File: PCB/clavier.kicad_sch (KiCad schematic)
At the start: 0 parts

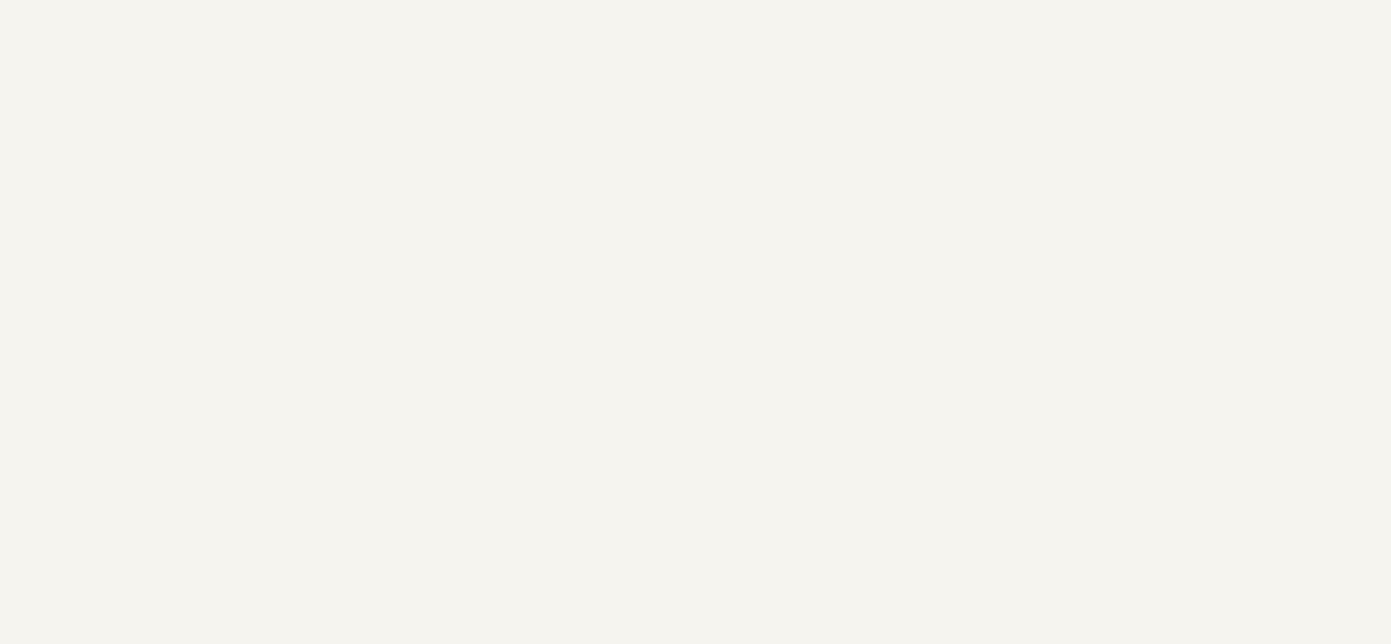
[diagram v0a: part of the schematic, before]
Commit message: Move the PCB files to a subfolder
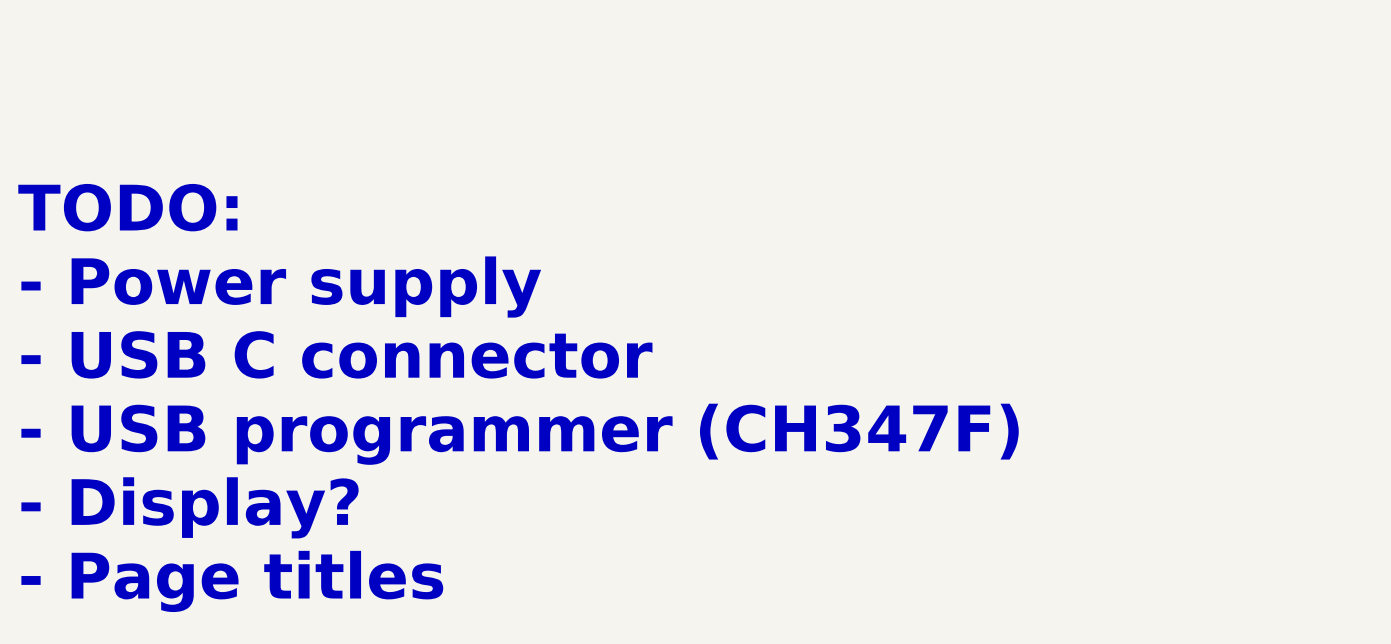
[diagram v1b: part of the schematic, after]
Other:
- note added: "TODO: - Power supply - USB C connector - USB programmer (CH347F) - Display? - Page titles"
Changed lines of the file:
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@@
 	(generator_version "9.0")
 	(paper "A4")
+	(text "TODO:\n- Power supply\n- USB C connector\n- USB programmer (CH347F)\n- Display?\n- Page titles"
+		(exclude_from_sim no)
+		(at 40.0 150.0 0)
+		(effects
+			(font
+				(size 5.08 5.08)
+				(thickness 1.016)
+				(bold yes)
+				(color 194 0 0 1)
+			)
+			(justify left)
+		)
+	)
 	(bus
 		(pts

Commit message: Add more TODOs
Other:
- added sheet Display (display.kicad_sch)
- added sheet Power (power.kicad_sch)
- added sheet USB (usb.kicad_sch)
- note added: "TODO schematics: - Power supply - LEDs - Test points - USB C connector - USB hub (GL852G-OHY60) - USB programmer (CH347F) - Display? - Page titles - Check licenses TODO layout: - Mounting holes - 3D models (all, including keycaps) - Alternate ctrl + odd/even number keys - Cat logo - Title block TODO release: - Export production files - Export PDF"
- note removed: "TODO: - Power supply - USB C connector - USB programmer (CH347F) - Display? - Page titles"
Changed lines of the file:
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@@
 	(generator_version "9.0")
 	(paper "A4")
-	(text "TODO:\n- Power supply\n- USB C connector\n- USB programmer (CH347F)\n- Display?\n- Page titles"
-		(exclude_from_sim no)
-		(at 40.0 150.0 0)
+	(text "TODO schematics:\n- Power supply\n- LEDs\n- Test points\n- USB C connector\n- USB hub (GL852G-OHY60)\n- USB programmer (CH347F)\n- Display?\n- Page titles\n- Check licenses\n\nTODO layout:\n- Mounting holes\n- 3D models (all, including keycaps)\n- Alternate ctrl + odd/even number keys\n- Cat logo\n- Title block\n\nTODO release:\n- Export production files\n- Export PDF"
+		(exclude_from_sim no)
+		(at 19.304 99.568 0)
 		(effects
 			(font
@@
 	(bus
 		(pts
-			(xy 127 80.01) (xy 165.1 80.01)
+			(xy 177.8 92.71) (xy 215.9 92.71)
 		)
 		(stroke
@@
 	(bus
 		(pts
-			(xy 127 85.09) (xy 165.1 85.09)
+			(xy 177.8 97.79) (xy 215.9 97.79)
 		)
 		(stroke
@@
 	)
 	(sheet
-		(at 165.1 76.2)
+		(at 190.5 38.1)
+		(size 12.7 12.7)
+		(exclude_from_sim no)
+		(in_bom yes)
+		(on_board yes)
+		(dnp no)
+		(fields_autoplaced yes)
+		(stroke
+			(width 0.1524)
+			(type solid)
+		)
+		(fill
+			(color 0 0 0 0.0000)
+		)
+		(property "Sheetname" "Power"
+			(at 190.5 37.3884 0)
+			(effects
+				(font
+					(size 1.27 1.27)
+				)
+				(justify left bottom)
+			)
+		)
+		(property "Sheetfile" "power.kicad_sch"
+			(at 190.5 51.3846 0)
+			(effects
+				(font
+					(size 1.27 1.27)
+				)
+				(justify left top)
+			)
+		)
+		(instances
+			(project "clavier"
+				(path "/6362c6e0-59ef-40d3-b6e0-7e9dfe7b9b20"
+					(page "8")
+				)
+			)
+		)
+	)
+	(sheet
+		(at 215.9 38.1)
+		(size 12.7 12.7)
+		(exclude_from_sim no)
+		(in_bom yes)
+		(on_board yes)
+		(dnp no)
+		(fields_autoplaced yes)
+		(stroke
+			(width 0.1524)
+			(type solid)
+		)
+		(fill
+			(color 0 0 0 0.0000)
+		)
+		(property "Sheetname" "Display"
+			(at 215.9 37.3884 0)
+			(effects
+				(font
+					(size 1.27 1.27)
+				)
+				(justify left bottom)
+			)
+		)
+		(property "Sheetfile" "display.kicad_sch"
+			(at 215.9 51.3846 0)
+			(effects
+				(font
+					(size 1.27 1.27)
+				)
+				(justify left top)
+			)
+		)
+		(instances
+			(project "clavier"
+				(path "/6362c6e0-59ef-40d3-b6e0-7e9dfe7b9b20"
+					(page "7")
+				)
+			)
+		)
+	)
+	(sheet
+		(at 215.9 88.9)
 		(size 25.4 12.7)
 		(exclude_from_sim no)
@@
 		)
 		(property "Sheetname" "FPGA"
-			(at 165.1 75.4884 0)
+			(at 215.9 88.1884 0)
 			(effects
 				(font
@@
 		)
 		(property "Sheetfile" "fpga.kicad_sch"
-			(at 165.1 89.4846 0)
+			(at 215.9 102.1846 0)
 			(effects
 				(font
@@
 		)
 		(pin "K{Keys}" input
-			(at 165.1 80.01 180)
+			(at 215.9 92.71 180)
 			(effects
 				(font
@@
 		)
 		(pin "Kp{KpKeys}" input
-			(at 165.1 85.09 180)
+			(at 215.9 97.79 180)
 			(effects
 				(font
@@
 			(project "clavier"
 				(path "/6362c6e0-59ef-40d3-b6e0-7e9dfe7b9b20"
+					(page "3")
+				)
+			)
+		)
+	)
+	(sheet
+		(at 165.1 38.1)
+		(size 12.7 12.7)
+		(exclude_from_sim no)
+		(in_bom yes)
+		(on_board yes)
+		(dnp no)
+		(fields_autoplaced yes)
+		(stroke
+			(width 0.1524)
+			(type solid)
+		)
+		(fill
+			(color 0 0 0 0.0000)
+		)
+		(property "Sheetname" "USB"
+			(at 165.1 37.3884 0)
+			(effects
+				(font
+					(size 1.27 1.27)
+				)
+				(justify left bottom)
+			)
+		)
+		(property "Sheetfile" "usb.kicad_sch"
+			(at 165.1 51.3846 0)
+			(effects
+				(font
+					(size 1.27 1.27)
+				)
+				(justify left top)
+			)
+		)
+		(instances
+			(project "clavier"
+				(path "/6362c6e0-59ef-40d3-b6e0-7e9dfe7b9b20"
 					(page "2")
 				)
@@
 	)
 	(sheet
-		(at 101.6 76.2)
+		(at 152.4 88.9)
 		(size 25.4 12.7)
 		(exclude_from_sim no)
@@
 		)
 		(property "Sheetname" "Keys"
-			(at 101.6 75.4884 0)
+			(at 152.4 88.1884 0)
 			(effects
 				(font
@@
 		)
 		(property "Sheetfile" "keys.kicad_sch"
-			(at 101.6 89.4846 0)
+			(at 152.4 102.1846 0)
 			(effects
 				(font
@@
 		)
 		(pin "Kp{KpKeys}" output
-			(at 127 85.09 0)
+			(at 177.8 97.79 0)
 			(effects
 				(font
@@
 		)
 		(pin "K{Keys}" output
-			(at 127 80.01 0)
+			(at 177.8 92.71 0)
 			(effects
 				(font
@@
 			(project "clavier"
 				(path "/6362c6e0-59ef-40d3-b6e0-7e9dfe7b9b20"
-					(page "5")
-				)
-			)
+					(page "6")
+				)
+			)

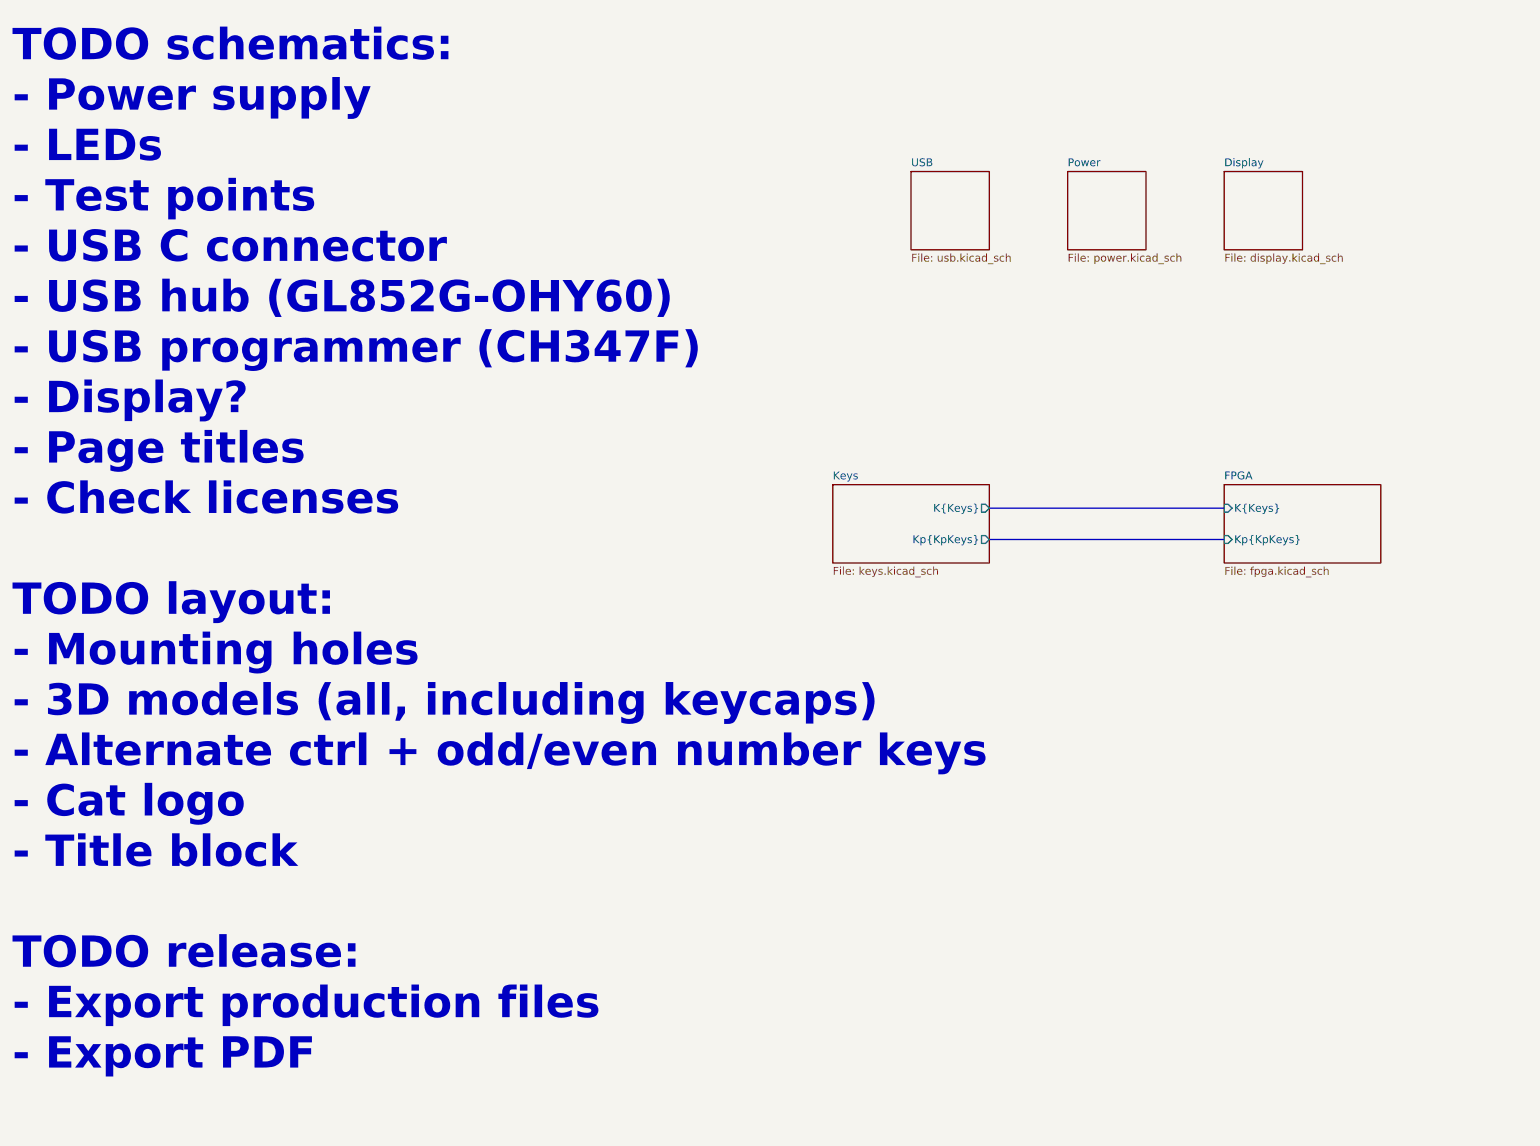
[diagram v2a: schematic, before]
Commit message: Add a USB hub
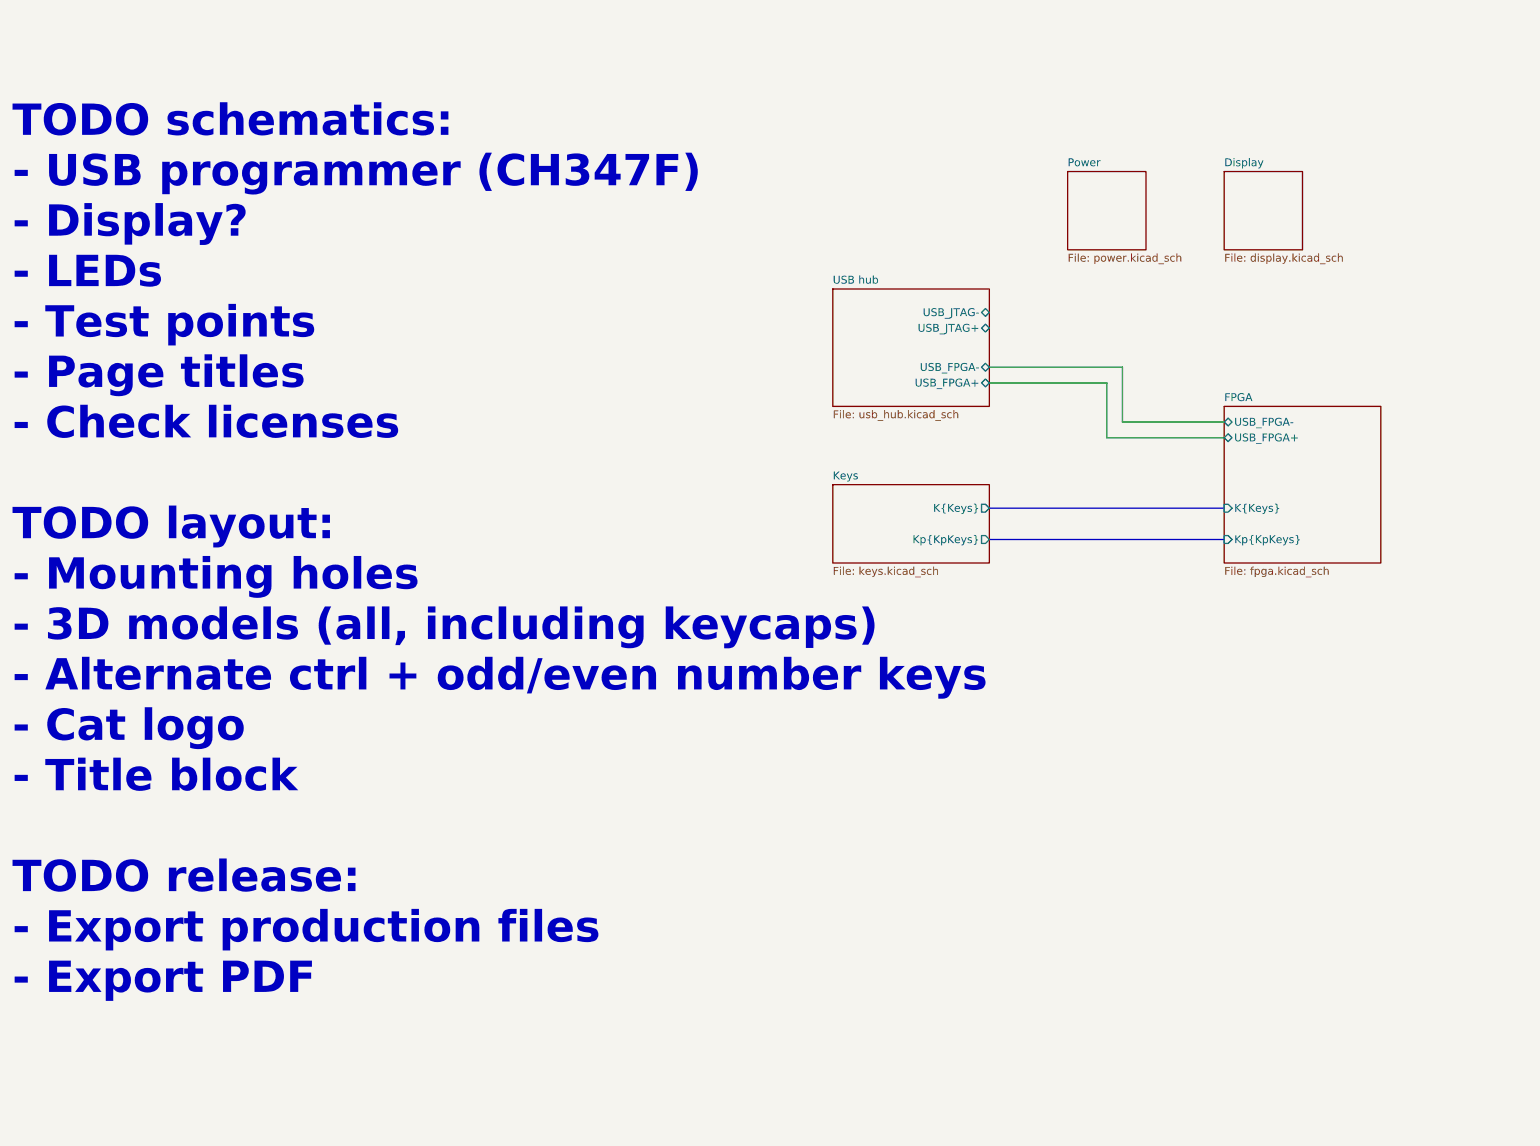
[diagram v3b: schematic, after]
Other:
- sheet USB renamed USB hub
- sheet FPGA ports: added USB_FPGA+, USB_FPGA-; removed none
- sheet USB hub: file usb.kicad_sch -> usb_hub.kicad_sch
- sheet USB hub ports: added USB_FPGA+, USB_FPGA-, USB_JTAG+, USB_JTAG-; removed none
- note added: "TODO schematics: - USB programmer (CH347F) - Display? - LEDs - Test points - Page titles - Check licenses TODO layout: - Mounting holes - 3D models (all, including keycaps) - Alternate ctrl + odd/even number keys - Cat logo - Title block TODO release: - Export production files - Export PDF"
- note removed: "TODO schematics: - Power supply - LEDs - Test points - USB C connector - USB hub (GL852G-OHY60) - USB programmer (CH347F) - Display? - Page titles - Check licenses TODO layout: - Mounting holes - 3D models (all, including keycaps) - Alternate ctrl + odd/even number keys - Cat logo - Title block TODO release: - Export production files - Export PDF"
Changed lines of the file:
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@@
 	(generator_version "9.0")
 	(paper "A4")
-	(text "TODO schematics:\n- Power supply\n- LEDs\n- Test points\n- USB C connector\n- USB hub (GL852G-OHY60)\n- USB programmer (CH347F)\n- Display?\n- Page titles\n- Check licenses\n\nTODO layout:\n- Mounting holes\n- 3D models (all, including keycaps)\n- Alternate ctrl + odd/even number keys\n- Cat logo\n- Title block\n\nTODO release:\n- Export production files\n- Export PDF"
+	(text "TODO schematics:\n- USB programmer (CH347F)\n- Display?\n- LEDs\n- Test points\n- Page titles\n- Check licenses\n\nTODO layout:\n- Mounting holes\n- 3D models (all, including keycaps)\n- Alternate ctrl + odd/even number keys\n- Cat logo\n- Title block\n\nTODO release:\n- Export production files\n- Export PDF"
 		(exclude_from_sim no)
 		(at 19.304 99.568 0)
@@
 		)
 	)
+	(wire
+		(pts
+			(xy 199.39 69.85) (xy 199.39 78.74)
+		)
+		(stroke
+			(width 0)
+			(type default)
+		)
+	)
+	(wire
+		(pts
+			(xy 177.8 72.39) (xy 196.85 72.39)
+		)
+		(stroke
+			(width 0)
+			(type default)
+		)
+	)
+	(wire
+		(pts
+			(xy 177.8 69.85) (xy 199.39 69.85)
+		)
+		(stroke
+			(width 0)
+			(type default)
+		)
+	)
+	(wire
+		(pts
+			(xy 196.85 72.39) (xy 196.85 81.28)
+		)
+		(stroke
+			(width 0)
+			(type default)
+		)
+	)
 	(bus
 		(pts
@@
 		)
 	)
+	(wire
+		(pts
+			(xy 199.39 78.74) (xy 215.9 78.74)
+		)
+		(stroke
+			(width 0)
+			(type default)
+		)
+	)
 	(bus
 		(pts
 			(xy 177.8 97.79) (xy 215.9 97.79)
+		)
+		(stroke
+			(width 0)
+			(type default)
+		)
+	)
+	(wire
+		(pts
+			(xy 196.85 81.28) (xy 215.9 81.28)
 		)
 		(stroke
@@
 	)
 	(sheet
-		(at 215.9 88.9)
-		(size 25.4 12.7)
+		(at 215.9 76.2)
+		(size 25.4 25.4)
 		(exclude_from_sim no)
 		(in_bom yes)
@@
 		)
 		(property "Sheetname" "FPGA"
-			(at 215.9 88.1884 0)
+			(at 215.9 75.4884 0)
 			(effects
 				(font
@@
 		(pin "Kp{KpKeys}" input
 			(at 215.9 97.79 180)
+			(effects
+				(font
+					(size 1.27 1.27)
+				)
+				(justify left)
+			)
+		)
+		(pin "USB_FPGA-" bidirectional
+			(at 215.9 78.74 180)
+			(effects
+				(font
+					(size 1.27 1.27)
+				)
+				(justify left)
+			)
+		)
+		(pin "USB_FPGA+" bidirectional
+			(at 215.9 81.28 180)
 			(effects
 				(font
@@
 	)
 	(sheet
-		(at 165.1 38.1)
-		(size 12.7 12.7)
+		(at 152.4 57.15)
+		(size 25.4 19.05)
 		(exclude_from_sim no)
 		(in_bom yes)
@@
 			(color 0 0 0 0.0000)
 		)
-		(property "Sheetname" "USB"
-			(at 165.1 37.3884 0)
+		(property "Sheetname" "USB hub"
+			(at 152.4 56.4384 0)
 			(effects
 				(font
@@
 			)
 		)
-		(property "Sheetfile" "usb.kicad_sch"
-			(at 165.1 51.3846 0)
+		(property "Sheetfile" "usb_hub.kicad_sch"
+			(at 152.4 76.7846 0)
 			(effects
 				(font
@@
 			)
 		)
+		(pin "USB_FPGA+" bidirectional
+			(at 177.8 72.39 0)
+			(effects
+				(font
+					(size 1.27 1.27)
+				)
+				(justify right)
+			)
+		)
+		(pin "USB_FPGA-" bidirectional
+			(at 177.8 69.85 0)
+			(effects
+				(font
+					(size 1.27 1.27)
+				)
+				(justify right)
+			)
+		)
+		(pin "USB_JTAG-" bidirectional
+			(at 177.8 60.96 0)
+			(effects
+				(font
+					(size 1.27 1.27)
+				)
+				(justify right)
+			)
+		)
+		(pin "USB_JTAG+" bidirectional
+			(at 177.8 63.5 0)
+			(effects
+				(font
+					(size 1.27 1.27)
+				)
+				(justify right)
+			)
+		)
